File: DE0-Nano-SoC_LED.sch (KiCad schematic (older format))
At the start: 70 parts, among them J1 Conn_02x08_Odd_Even, J10 Conn_01x08, J11 Conn_01x01, J12 Conn_01x01, J13 Conn_01x01, J14 Conn_01x01, J15 Conn_01x01, J16 Conn_01x10, J17 Conn_01x08, J18 Conn_01x01, J19 Conn_01x01, J2 Conn_02x08_Odd_Even, J3 Conn_02x20_Odd_Even, J4 Conn_02x20_Odd_Even, J5 Conn_02x08_Odd_Even, J6 Conn_02x08_Odd_Even, J7 Conn_02x08_Odd_Even, J8 Conn_01x01, J9 Conn_01x06, U1 74HC245, U10 74HC245, U2 74HC245, U3 74HC245, U4 74HC245, U5 74HC245, U6 74HC245, U7 74HC245, U8 74HC245, U9 74HC245

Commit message: almost all components
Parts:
- added J20, J21, J22, J23, J24: Conn_02x08_Odd_Even, Connectors_Multicomp:Multicomp_MC9A12-1634_2x08x2.54mm_Straight, symbol Conn_02x08_Odd_Even
- added RN21, RN22, RN23, RN24, RN25, RN26, RN27, RN28, RN29, RN30, RN31, RN32, RN33, RN34, RN35, RN36, RN37, RN38, RN39, RN40: R_Pack04, Resistors_SMD:R_Array_Concave_4x0402, symbol R_Pack04
- added U11, U12, U13, U14, U15, U16, U17, U18, U19, U20: 74HC245, SMD_Packages:SSOP-20, symbol 74HC245
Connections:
- net labels added: A_10_2, A_9_2, B1_10_2, B1_9_2, B2_10_2, B2_9_2, B_10_2, B_9_2, CLK_10_2, CLK_9_2, C_10_2, C_9_2, D_10_2, D_9_2, G1_10_2, G1_9_2, G2_10_2, G2_9_2, LAT_10_2, LAT_9_2, OE_10_2, OE_9_2, R1_10_2, R1_9_2, R2_10_2, R2_9_2
- wire segments 512 -> 887

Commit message: pin rename
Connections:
- net labels added: A_6_2, A_7_2, A_8_2, B1_6_2, B1_7_2, B1_8_2, B2_6_2, B2_7_2, B2_8_2, B_6_2, B_7_2, B_8_2, CLK_6_2, CLK_7_2, CLK_8_2, C_6_2, C_7_2, C_8_2, D_6_2, D_7_2, D_8_2, G1_6_2, G1_7_2, G1_8_2, G2_6_2, G2_7_2, G2_8_2, LAT_6_2, LAT_7_2, LAT_8_2, OE_6_2, OE_7_2, OE_8_2, R1_6_2, R1_7_2, R1_8_2, R2_6_2, R2_7_2, R2_8_2

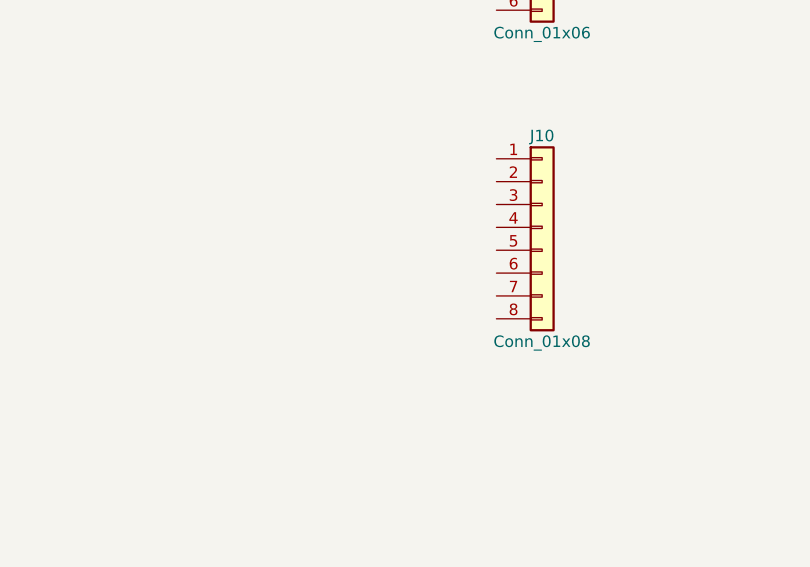
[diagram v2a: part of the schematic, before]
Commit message: small pcb fix
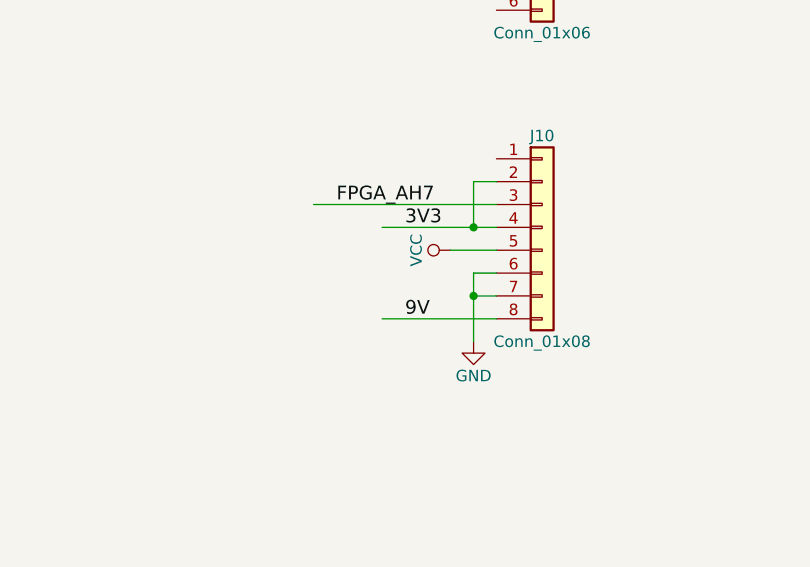
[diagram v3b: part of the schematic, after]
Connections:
- net labels added: 9V, FPGA_AH7
- wire segments 887 -> 896
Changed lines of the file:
@@
 	18000 12850 18000 12750
 Connection ~ 18550 12750
+$Comp
+L GND #PWR?
+U 1 1 5A5FC006
+P 8950 8450
+F 0 "#PWR?" H 8950 8200 50  0001 C CNN
+F 1 "GND" H 8950 8300 50  0000 C CNN
+F 2 "" H 8950 8450 50  0001 C CNN
+F 3 "" H 8950 8450 50  0001 C CNN
+	1    8950 8450
+	1    0    0    -1
+$EndComp
+Wire Wire Line
+	9050 8150 8950 8150
+Wire Wire Line
+	8950 8150 8950 8450
+Wire Wire Line
+	9050 8250 8950 8250
+Connection ~ 8950 8250
+Wire Wire Line
+	9050 8350 8550 8350
+Text Label 8650 8350 0    60   ~ 0
+9V
+$Comp
+L VCC #PWR?
+U 1 1 5A5FF374
+P 8850 8050
+F 0 "#PWR?" H 8850 7900 50  0001 C CNN
+F 1 "VCC" H 8850 8200 50  0000 C CNN
+F 2 "" H 8850 8050 50  0001 C CNN
+F 3 "" H 8850 8050 50  0001 C CNN
+	1    8850 8050
+	0    -1   -1   0
+$EndComp
+Wire Wire Line
+	8850 8050 9050 8050
+Wire Wire Line
+	8550 7950 9050 7950
+Wire Wire Line
+	8950 7950 8950 7750
+Wire Wire Line
+	8950 7750 9050 7750
+Connection ~ 8950 7950
+Text Label 8650 7950 0    60   ~ 0
+3V3
+Wire Wire Line
+	9050 7850 8250 7850
+Text Label 8350 7850 0    60   ~ 0
+FPGA_AH7
 $EndSCHEMATC

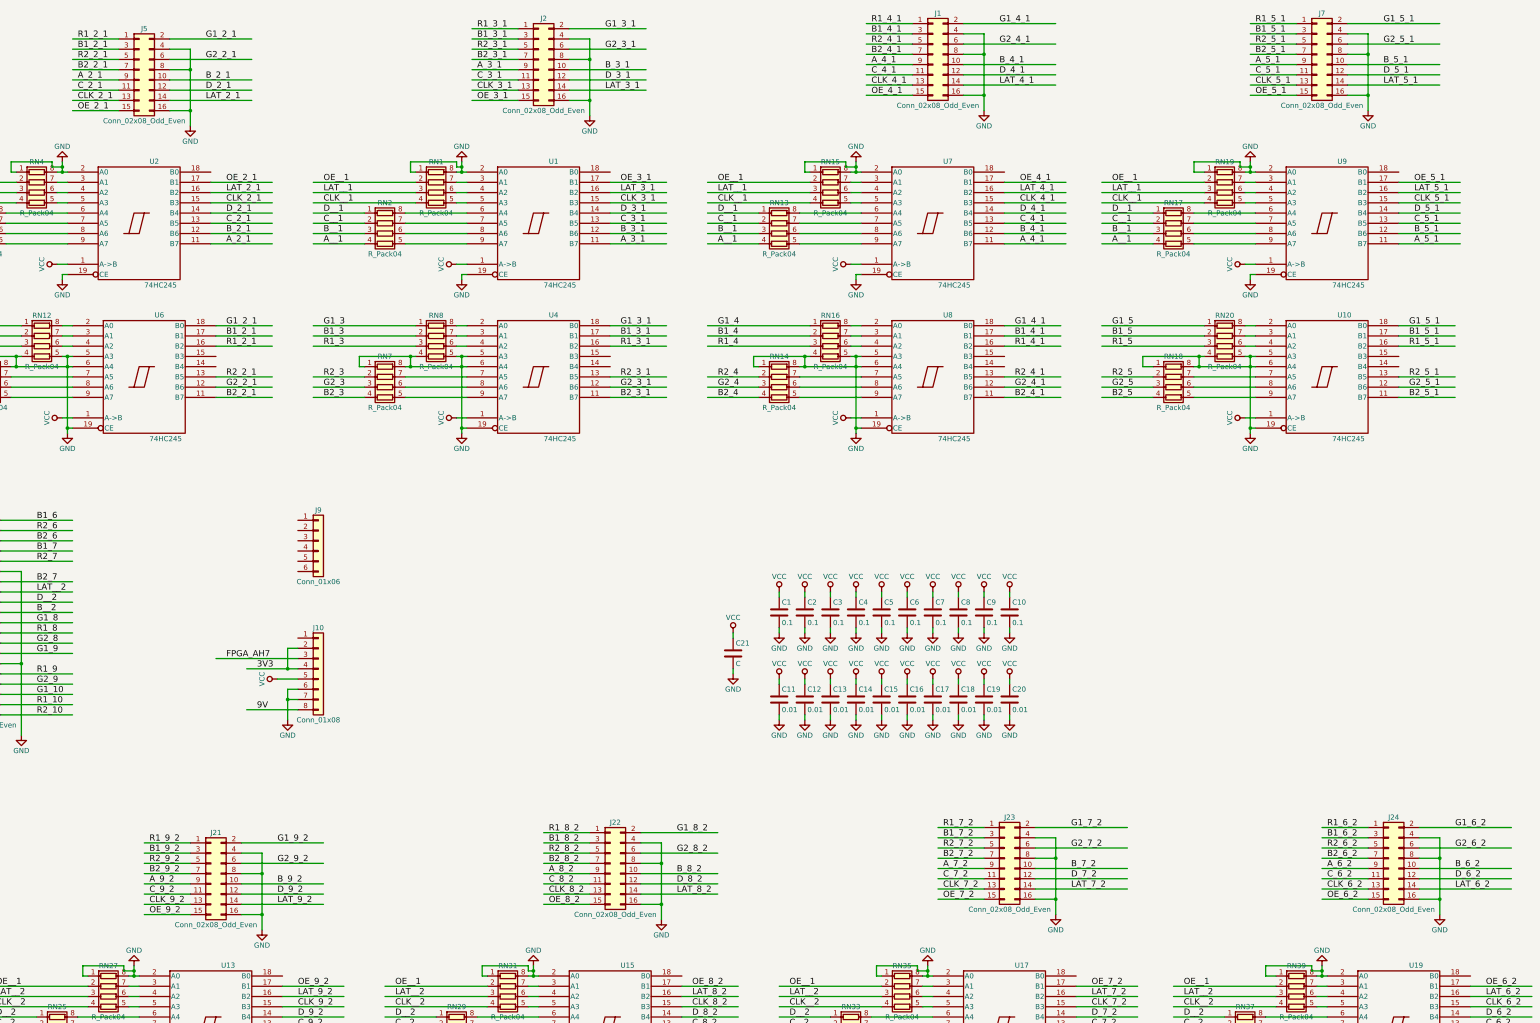
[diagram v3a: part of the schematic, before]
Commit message: components placement continue
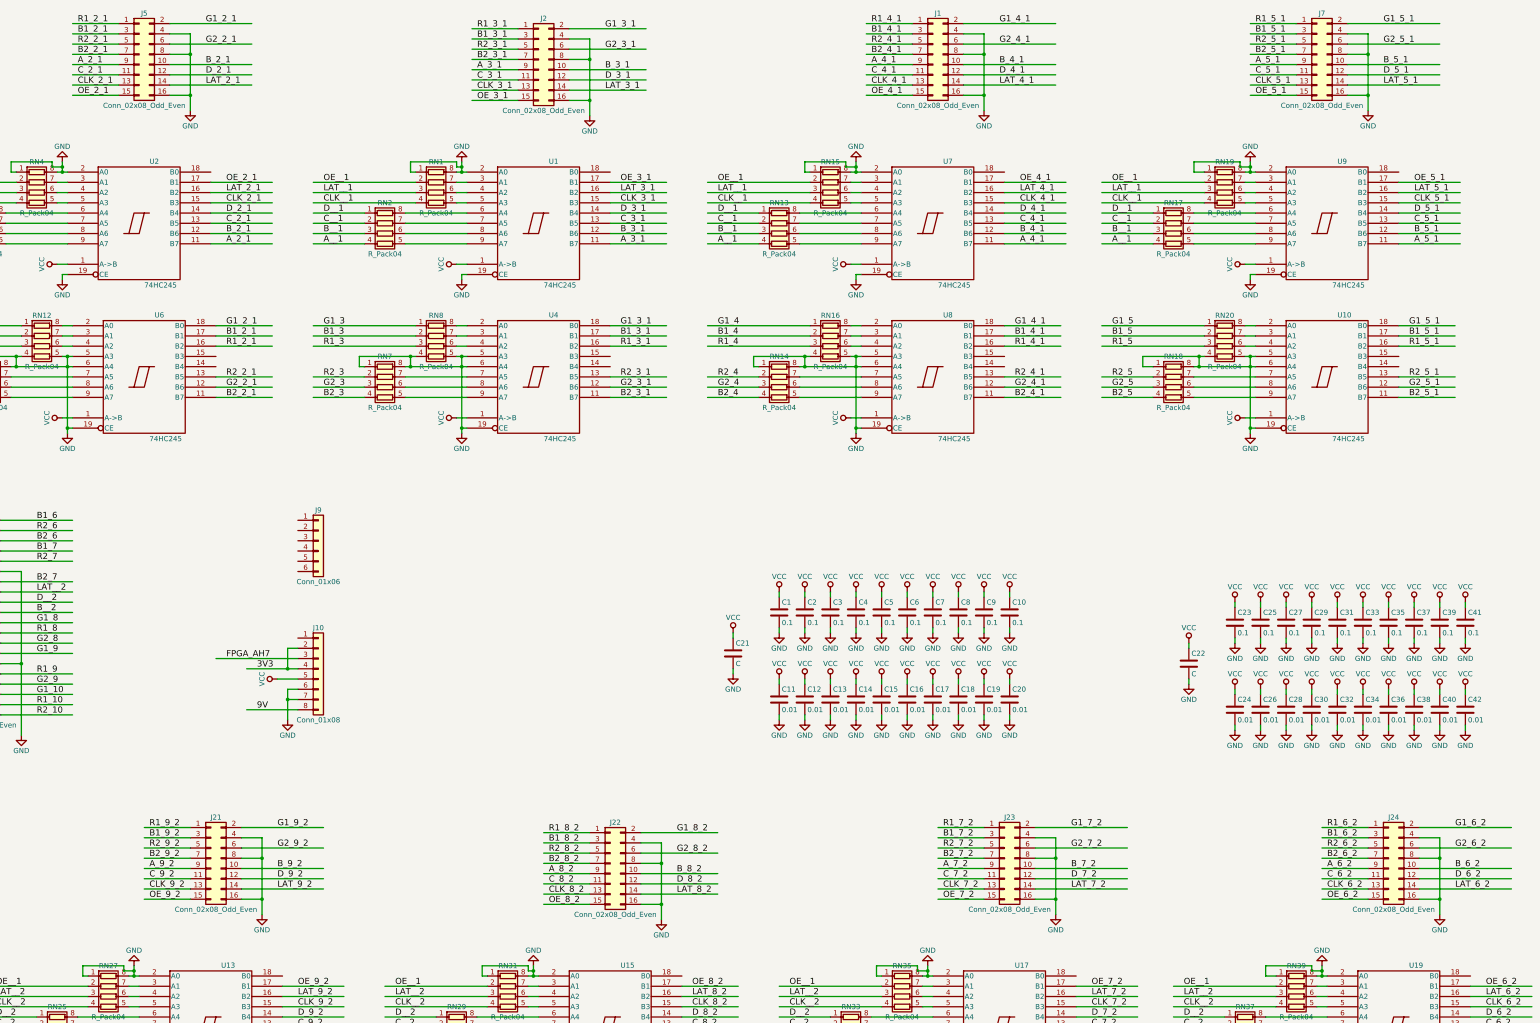
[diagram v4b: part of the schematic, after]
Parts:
- added C22: C, Capacitors_SMD:C_1210, symbol C
- added C23, C25, C27, C29, C31, C33, C35, C37, C39, C41: 0.1, Capacitors_SMD:C_0402_NoSilk, symbol C
- added C24, C26, C28, C30, C32, C34, C36, C38, C40, C42: 0.01, Capacitors_SMD:C_0402_NoSilk, symbol C
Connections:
- wire segments 896 -> 938
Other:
- moved on the sheet: J21, J5

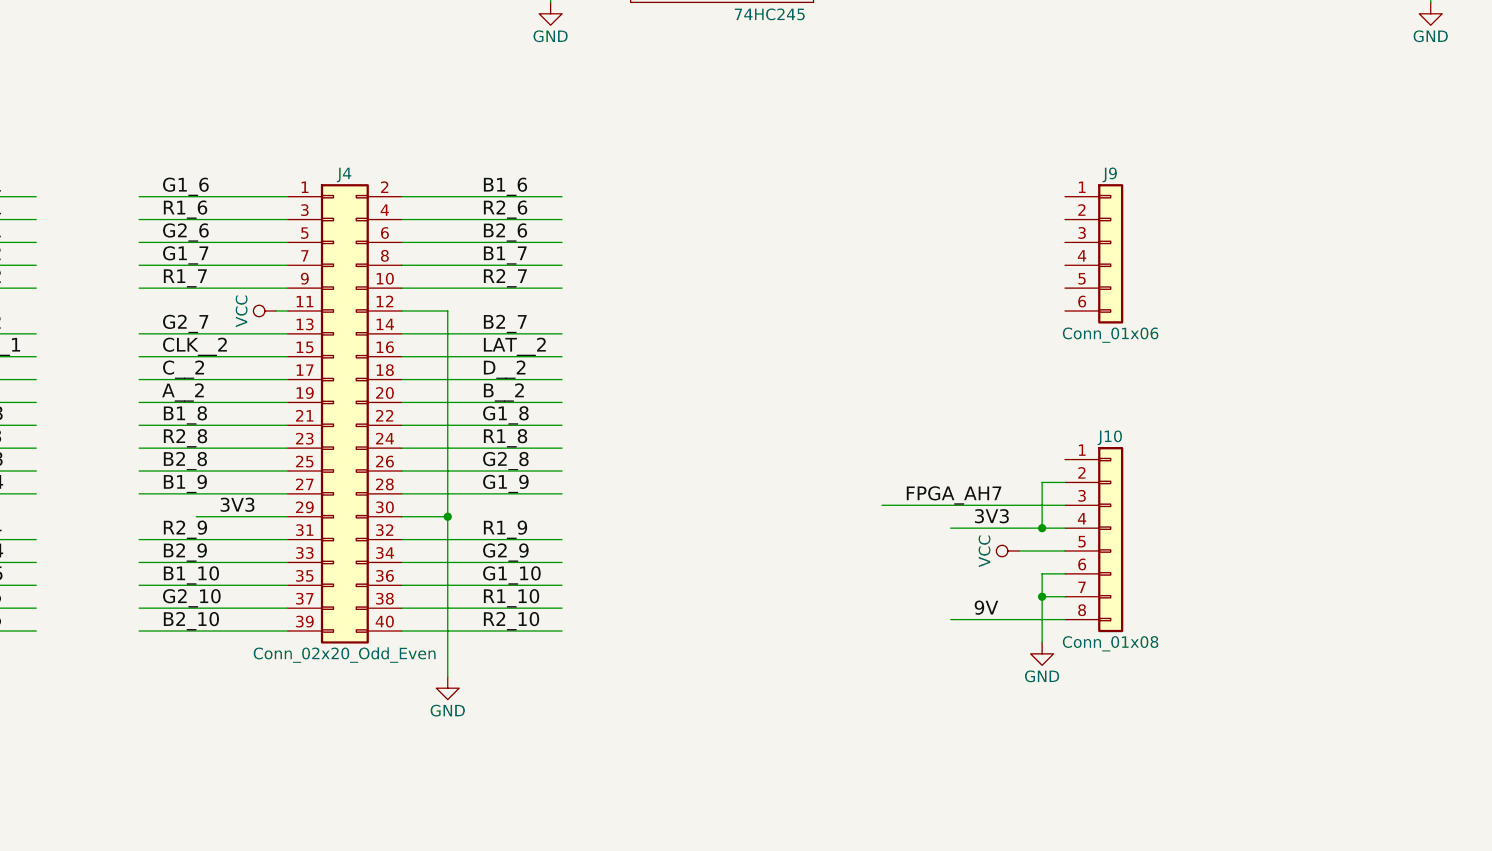
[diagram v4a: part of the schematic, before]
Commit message: pin swapping
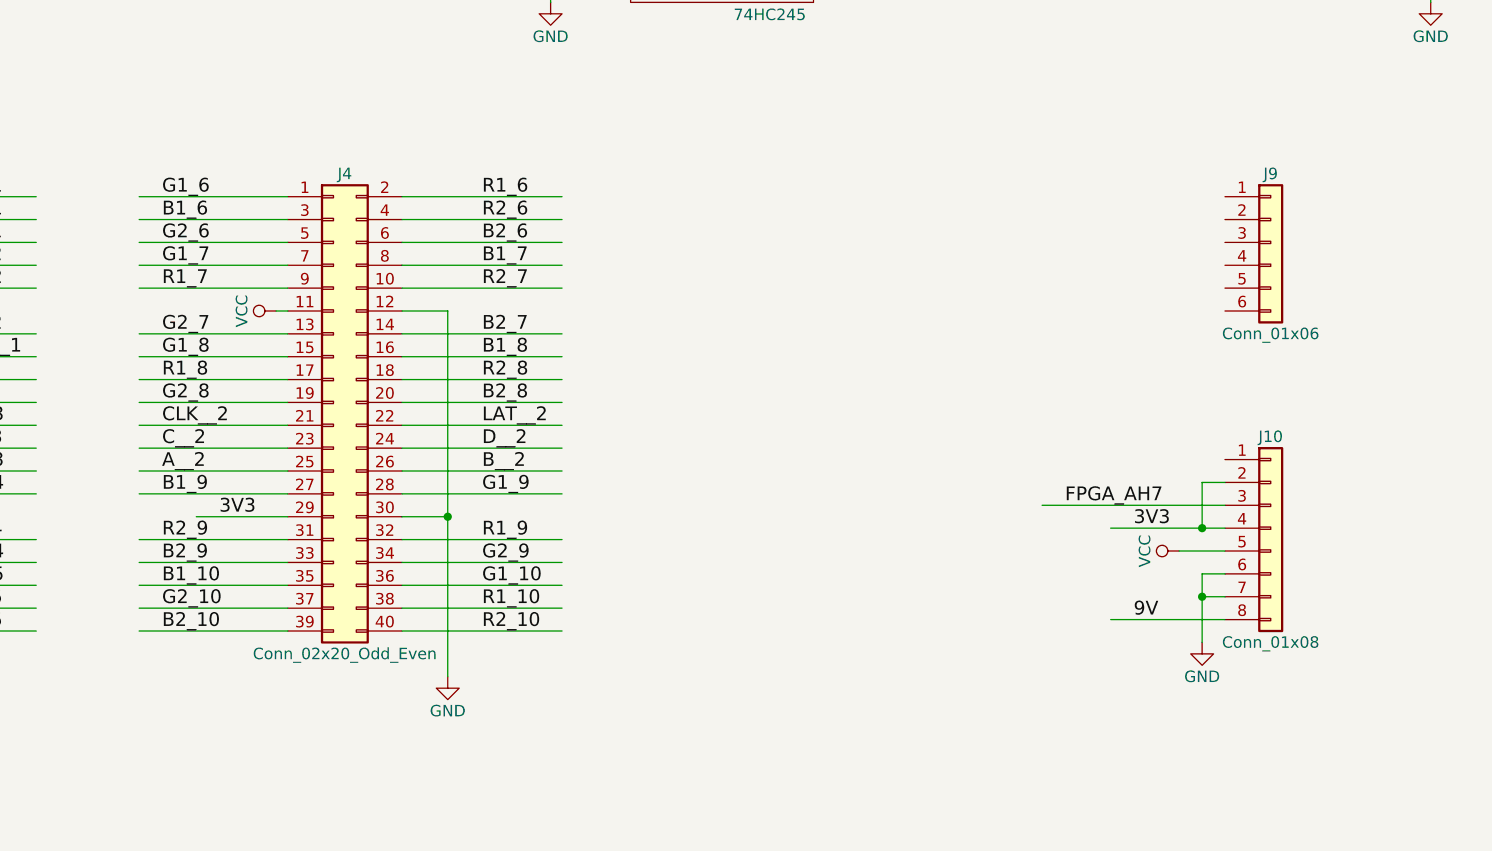
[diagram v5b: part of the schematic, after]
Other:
- moved on the sheet: J10, J9
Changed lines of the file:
@@
 L Conn_01x08 J10
 U 1 1 5A5F75CF
-P 9250 7950
-F 0 "J10" H 9250 8350 50  0000 C CNN
-F 1 "Conn_01x08" H 9250 7450 50  0000 C CNN
-F 2 "Pin_Headers:Pin_Header_Straight_1x08_Pitch2.54mm" H 9250 7950 50  0001 C CNN
-F 3 "" H 9250 7950 50  0001 C CNN
-	1    9250 7950
+P 9950 7950
+F 0 "J10" H 9950 8350 50  0000 C CNN
+F 1 "Conn_01x08" H 9950 7450 50  0000 C CNN
+F 2 "Pin_Headers:Pin_Header_Straight_1x08_Pitch2.54mm" H 9950 7950 50  0001 C CNN
+F 3 "" H 9950 7950 50  0001 C CNN
+	1    9950 7950
 	1    0    0    -1
 $EndComp
@@
 	5650 7700 5000 7700
 Text Label 6500 7400 0    60   ~ 0
-B__2
+B2_8
 Wire Wire Line
 	6150 7300 6850 7300
@@
 	6150 7100 6850 7100
 Text Label 5100 7200 0    60   ~ 0
-CLK__2
+G1_8
 Text Label 6500 7200 0    60   ~ 0
-LAT__2
+B1_8
 Text Label 5100 7300 0    60   ~ 0
-C__2
+R1_8
 Text Label 6500 7300 0    60   ~ 0
-D__2
+R2_8
 Text Label 5100 7400 0    60   ~ 0
-A__2
+G2_8
 Wire Wire Line
 	5650 6500 5000 6500
@@
 B2_7
 Text Label 5100 7500 0    60   ~ 0
-B1_8
+CLK__2
 Text Label 6500 7500 0    60   ~ 0
-G1_8
+LAT__2
 Text Label 5100 7600 0    60   ~ 0
-R2_8
+C__2
 Text Label 6500 7600 0    60   ~ 0
-R1_8
+D__2
 Text Label 5100 7700 0    60   ~ 0
-B2_8
+A__2
 Text Label 6500 7700 0    60   ~ 0
-G2_8
+B__2
 Wire Wire Line
 	5650 7800 5000 7800
@@
 G2_9
 Text Label 6500 6500 0    60   ~ 0
-B1_6
+R1_6
 Text Label 5100 6900 0    60   ~ 0
 R1_7
@@
 G2_6
 Text Label 5100 6600 0    60   ~ 0
-R1_6
+B1_6
 Text Label 5100 6500 0    60   ~ 0
 G1_6
@@
 L Conn_01x06 J9
 U 1 1 5A5FD2C9
-P 9250 6700
-F 0 "J9" H 9250 7000 50  0000 C CNN
-F 1 "Conn_01x06" H 9250 6300 50  0000 C CNN
-F 2 "Pin_Headers:Pin_Header_Straight_1x06_Pitch2.54mm" H 9250 6700 50  0001 C CNN
-F 3 "" H 9250 6700 50  0001 C CNN
-	1    9250 6700
+P 9950 6700
+F 0 "J9" H 9950 7000 50  0000 C CNN
+F 1 "Conn_01x06" H 9950 6300 50  0000 C CNN
+F 2 "Pin_Headers:Pin_Header_Straight_1x06_Pitch2.54mm" H 9950 6700 50  0001 C CNN
+F 3 "" H 9950 6700 50  0001 C CNN
+	1    9950 6700
 	1    0    0    -1
 $EndComp
@@
 L GND #PWR0110
 U 1 1 5A5FC006
-P 8950 8450
-F 0 "#PWR0110" H 8950 8200 50  0001 C CNN
-F 1 "GND" H 8950 8300 50  0000 C CNN
-F 2 "" H 8950 8450 50  0001 C CNN
-F 3 "" H 8950 8450 50  0001 C CNN
-	1    8950 8450
-	1    0    0    -1
-$EndComp
-Wire Wire Line
-	9050 8150 8950 8150
-Wire Wire Line
-	8950 8150 8950 8450
-Wire Wire Line
-	9050 8250 8950 8250
-Connection ~ 8950 8250
-Wire Wire Line
-	9050 8350 8550 8350
-Text Label 8650 8350 0    60   ~ 0
+P 9650 8450
+F 0 "#PWR0110" H 9650 8200 50  0001 C CNN
+F 1 "GND" H 9650 8300 50  0000 C CNN
+F 2 "" H 9650 8450 50  0001 C CNN
+F 3 "" H 9650 8450 50  0001 C CNN
+	1    9650 8450
+	1    0    0    -1
+$EndComp
+Wire Wire Line
+	9750 8150 9650 8150
+Wire Wire Line
+	9650 8150 9650 8450
+Wire Wire Line
+	9750 8250 9650 8250
+Connection ~ 9650 8250
+Wire Wire Line
+	9750 8350 9250 8350
+Text Label 9350 8350 0    60   ~ 0
 9V
 $Comp
 L VCC #PWR0111
 U 1 1 5A5FF374
-P 8850 8050
-F 0 "#PWR0111" H 8850 7900 50  0001 C CNN
-F 1 "VCC" H 8850 8200 50  0000 C CNN
-F 2 "" H 8850 8050 50  0001 C CNN
-F 3 "" H 8850 8050 50  0001 C CNN
-	1    8850 8050
+P 9550 8050
+F 0 "#PWR0111" H 9550 7900 50  0001 C CNN
+F 1 "VCC" H 9550 8200 50  0000 C CNN
+F 2 "" H 9550 8050 50  0001 C CNN
+F 3 "" H 9550 8050 50  0001 C CNN
+	1    9550 8050
 	0    -1   -1   0
 $EndComp
 Wire Wire Line
-	8850 8050 9050 8050
-Wire Wire Line
-	8550 7950 9050 7950
-Wire Wire Line
-	8950 7950 8950 7750
-Wire Wire Line
-	8950 7750 9050 7750
-Connection ~ 8950 7950
-Text Label 8650 7950 0    60   ~ 0
+	9550 8050 9750 8050
+Wire Wire Line
+	9250 7950 9750 7950
+Wire Wire Line
+	9650 7950 9650 7750
+Wire Wire Line
+	9650 7750 9750 7750
+Connection ~ 9650 7950
+Text Label 9350 7950 0    60   ~ 0
 3V3
 Wire Wire Line
-	9050 7850 8250 7850
-Text Label 8350 7850 0    60   ~ 0
+	9750 7850 8950 7850
+Text Label 9050 7850 0    60   ~ 0
 FPGA_AH7
 $Comp

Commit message: some progress on pcb
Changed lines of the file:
@@
 	5650 6700 5000 6700
 Text Label 6500 6600 0    60   ~ 0
-R2_6
+R1_6
 Text Label 6500 6700 0    60   ~ 0
 B2_6
@@
 G2_9
 Text Label 6500 6500 0    60   ~ 0
-R1_6
+R2_6
 Text Label 5100 6900 0    60   ~ 0
 R1_7
@@
 G2_6
 Text Label 5100 6600 0    60   ~ 0
+G1_6
+Text Label 5100 6500 0    60   ~ 0
 B1_6
-Text Label 5100 6500 0    60   ~ 0
-G1_6
 $Comp
 L Conn_01x06 J9

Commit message: 2 unconnected nets remain
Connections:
- net labels added: OE__2
- net labels removed: FPGA_AH7
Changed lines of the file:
@@
 LAT__2
 Text Label 10000 11050 0    60   ~ 0
-OE__1
+OE__2
 $Comp
 L R_Pack04 RN25
@@
 LAT__2
 Text Label 6100 11050 0    60   ~ 0
-OE__1
+OE__2
 Wire Wire Line
 	8900 11050 9500 11050
@@
 LAT__2
 Text Label 2200 11050 0    60   ~ 0
-OE__1
+OE__2
 Wire Wire Line
 	5000 11050 5600 11050
@@
 LAT__2
 Text Label 13850 11050 0    60   ~ 0
-OE__1
+OE__2
 Wire Wire Line
 	16650 11050 17250 11050
@@
 LAT__2
 Text Label 17700 11050 0    60   ~ 0
-OE__1
+OE__2
 Wire Wire Line
 	20500 11050 21100 11050
@@
 	9750 7850 8950 7850
 Text Label 9050 7850 0    60   ~ 0
-FPGA_AH7
+OE__2
 $Comp
 L C C23

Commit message: silk and logo added, gerber generated
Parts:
- added J?: Conn_01x05, symbol Conn_01x05
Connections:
- wire segments 938 -> 948
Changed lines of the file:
@@
 	1    0    0    -1
 $EndComp
+$Comp
+L Conn_01x05 J?
+U 1 1 5A68BFF0
+P 1600 9100
+F 0 "J?" H 1600 9400 50  0000 C CNN
+F 1 "Conn_01x05" H 1600 8800 50  0000 C CNN
+F 2 "" H 1600 9100 50  0001 C CNN
+F 3 "" H 1600 9100 50  0001 C CNN
+	1    1600 9100
+	-1   0    0    -1
+$EndComp
+$Comp
+L GND #PWR?
+U 1 1 5A68CF92
+P 1900 9400
+F 0 "#PWR?" H 1900 9150 50  0001 C CNN
+F 1 "GND" H 1900 9250 50  0000 C CNN
+F 2 "" H 1900 9400 50  0001 C CNN
+F 3 "" H 1900 9400 50  0001 C CNN
+	1    1900 9400
+	1    0    0    -1
+$EndComp
+$Comp
+L VCC #PWR?
+U 1 1 5A68D493
+P 1900 8800
+F 0 "#PWR?" H 1900 8650 50  0001 C CNN
+F 1 "VCC" H 1900 8950 50  0000 C CNN
+F 2 "" H 1900 8800 50  0001 C CNN
+F 3 "" H 1900 8800 50  0001 C CNN
+	1    1900 8800
+	1    0    0    -1
+$EndComp
+Wire Wire Line
+	1800 8900 1900 8900
+Wire Wire Line
+	1900 8900 1900 8800
+Wire Wire Line
+	1800 9300 1900 9300
+Wire Wire Line
+	1900 9300 1900 9400
+Wire Wire Line
+	1800 8250 2300 8250
+Wire Wire Line
+	1800 8350 2300 8350
+Wire Wire Line
+	1800 8450 2300 8450
+Wire Wire Line
+	1800 9000 2300 9000
+Wire Wire Line
+	1800 9100 2300 9100
+Wire Wire Line
+	1800 9200 2300 9200
 $EndSCHEMATC
